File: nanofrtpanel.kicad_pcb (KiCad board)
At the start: 2 copper layers, 119.1 x 41.7 mm, 12 parts, among them P1 CONN_02X08, Q1 BS170, SW1 DOWN, SW2 UP, SW3 SELECT, SW4 ESC, SW5 RESET

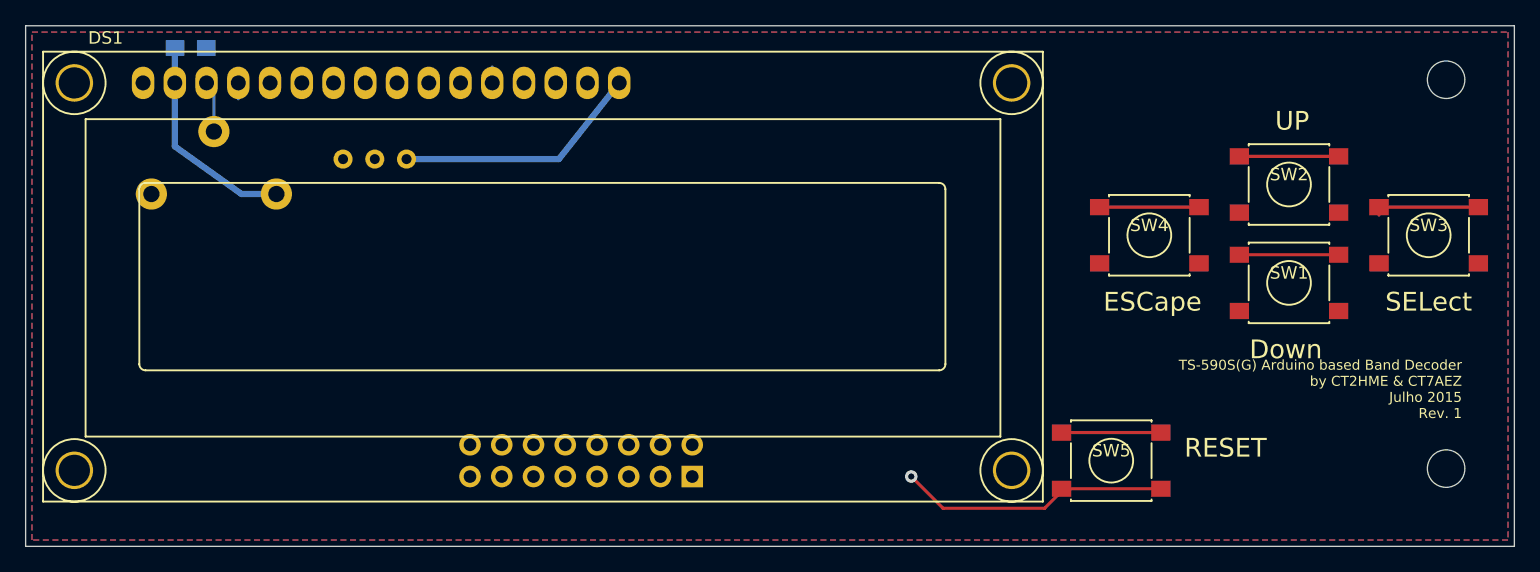
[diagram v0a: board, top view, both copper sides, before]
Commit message: Better access to RV1 and rebuild to be compatible.
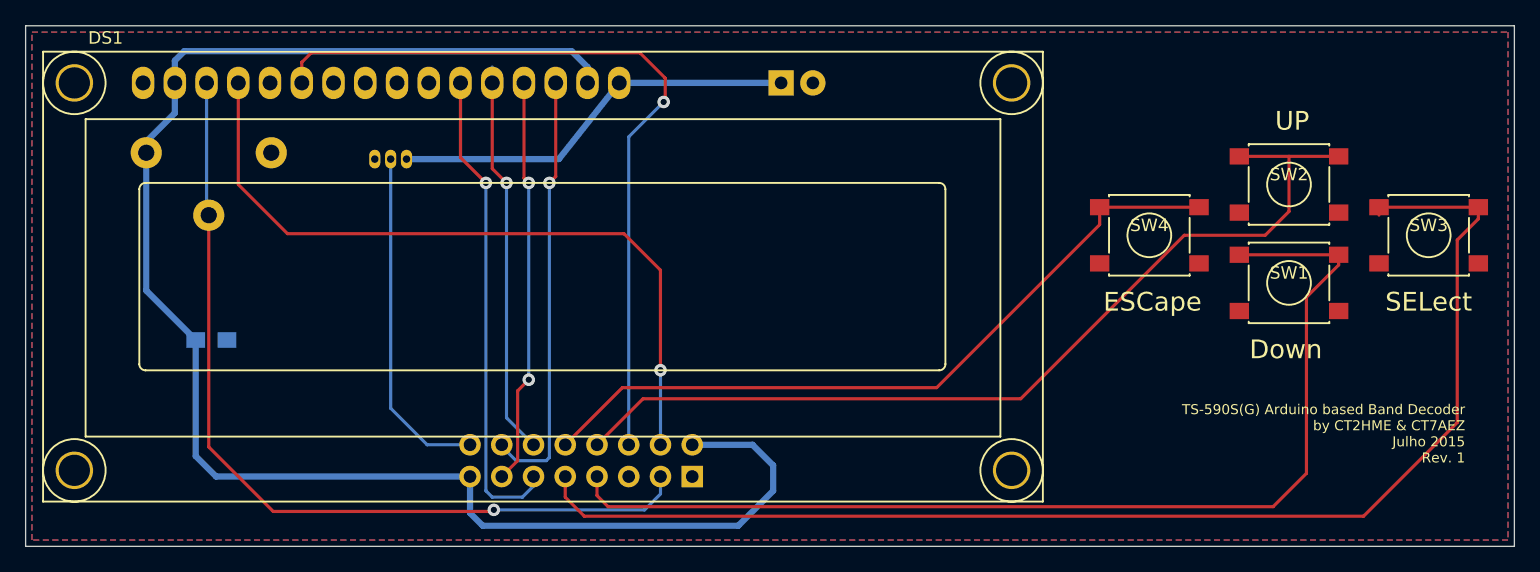
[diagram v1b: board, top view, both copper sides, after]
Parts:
- removed REF** (x2): MountingHole_3mm, Mounting_Holes:MountingHole_3mm
- removed SW5: RESET, Buttons_Switches_SMD:SW_SPST_PTS645
- added JP1: Jumper_NO_Small, Pin_Headers:Pin_Header_Straight_1x02, B.Cu at (125.2, 54.9)
- Q1: footprint Housings_TO-92:TO-92_Inline_Wide -> Housings_TO-92:TO-92_Inline_Narrow_Oval
- moved C1 23.4 mm to (79.6, 75.4)
- moved RV1 10.9 mm to (74.4, 60.5), turned to 0 degrees
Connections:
- DS1 pad 11: /D5a -> /D5
- DS1 pad 12: /D4a -> /D4
- DS1 pad 13: /D3a -> /D3
- DS1 pad 14: /D2a -> /D2
- DS1 pad 4: /D12a -> /D12
- DS1 pad 6: /D11a -> /D11
- P1 pad 1: +5V -> GND
- P1 pad 10: /RESETa -> /SW4
- P1 pad 11: /SW3a -> /D5
- P1 pad 12: /SW4a -> /D4
- P1 pad 13: /BCKL -> /D3
- P1 pad 14: GND -> /D2
- P1 pad 15: (no net) -> +5V
- P1 pad 16: (no net) -> /BCKL
- P1 pad 2: /D12a -> +5V
- P1 pad 3: /D11a -> /VO
- P1 pad 4: /D5a -> /D12
- P1 pad 5: /D4a -> GND
- P1 pad 6: /D3a -> /D11
- P1 pad 7: /D2a -> /SW1
- P1 pad 8: /SW1a -> /SW2
- P1 pad 9: /SW2a -> /SW3
- SW1 pad 1: /SW1a -> /SW1
- SW2 pad 1: /SW2a -> /SW2
- SW3 pad 1: /SW3a -> /SW3
- SW4 pad 1: /SW4a -> /SW4
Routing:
- net +5V: track 17.2 -> 129.9 mm
- net /SW3: track 0.00 -> 103.5 mm
- net /SW1: track 0.00 -> 86.5 mm
- net /SW2: track 0.00 -> 75.5 mm
- net /VO: track 4.13 -> 70.5 mm, vias 0 -> 1
- net /D11: track 0.00 -> 62.9 mm, vias 0 -> 1
- net /D12: track 0.00 -> 60.0 mm, vias 0 -> 1
- net /SW4: track 0.00 -> 59.4 mm
- net /D5: track 0.00 -> 38.9 mm, vias 0 -> 1
- net /D2: track 0.00 -> 34.7 mm, vias 0 -> 1
- net /D3: track 0.00 -> 32.5 mm, vias 0 -> 2
- net /D4: track 0.00 -> 31.6 mm, vias 0 -> 1
- net /BCKL: track 0.25 -> 27.5 mm
- net GND: track 23.2 -> 1.20 mm, vias 1 -> 0
- net Net-(DS1-Pad16): track 20.0 -> 32.9 mm
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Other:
- board text removed: "RESET"

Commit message: silkscreen update
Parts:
- added REF**: Symbol_OSHW-Logo_SilkScreen, Symbols:Symbol_OSHW-Logo_SilkScreen, F.Cu at (177.3, 55.2)
- added REF**: Symbol_OSHW-Logo_SilkScreen, Symbols:Symbol_OSHW-Logo_SilkScreen, B.Cu at (127.3, 69.2)
